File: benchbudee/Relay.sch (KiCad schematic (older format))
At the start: 0 parts

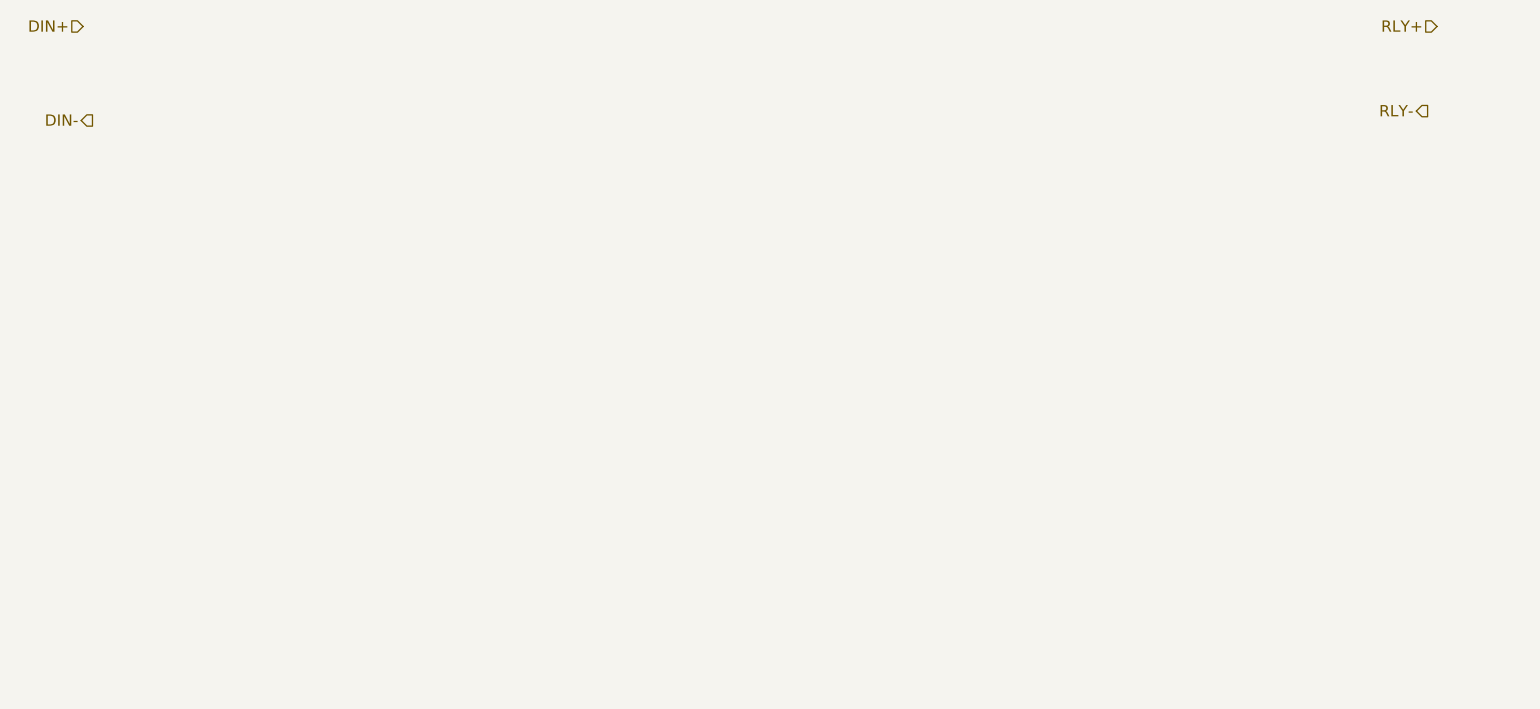
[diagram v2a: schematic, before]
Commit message: Added first pass at the relay module.
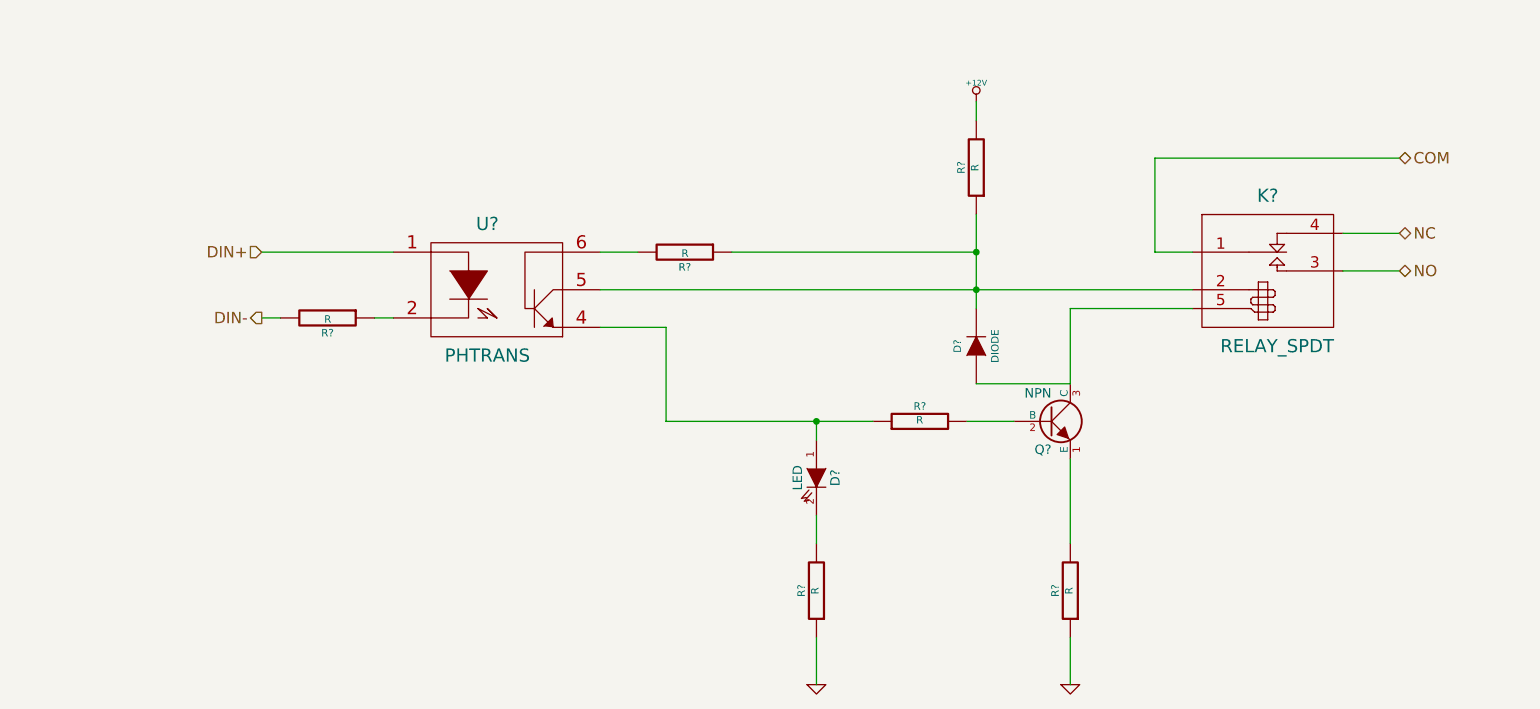
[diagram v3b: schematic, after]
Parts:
- added D?: LED, ~, symbol LED
- added D?: DIODE, ~, symbol DIODE
- added K?: RELAY_SPDT, ~, symbol RELAY_SPDT
- added Q?: NPN, ~, symbol NPN
- added R? (x6): R, ~, symbol R
- added U?: PHTRANS, ~, symbol PHTRANS
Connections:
- net DIN+: now also U?.1
- net DIN-: now also R?.2
- new net: R?.1, U?.2
- new net: D?.1 (A), R?.1, U?.4
- new net: D?.2 (K), K?.2 (COIL+), R?.1, R?.1, U?.5
- new net: R?.2, U?.6
- new net: Q?.2 (B), R?.2
- new net: Q?.1 (E), R?.2
- new net: D?.1 (A), K?.5 (COIL-), Q?.3 (C)
- new net: D?.2 (K), R?.2
- new net +12V: R?.2
- new net COM: K?.1 (COM)
- new net GND: R?.1, R?.1
- new net NC: K?.4 (NC)
- new net NO: K?.3 (NO)
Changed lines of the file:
@@
 LIBS:contrib
 LIBS:valves
+LIBS:benchbudee-custom
 LIBS:benchbudee-cache
 EELAYER 27 0
@@
 Comment4 ""
 $EndDescr
-Text HLabel 9050 1700 0    60   Input ~ 0
-RLY+
-Text HLabel 9000 2150 0    60   Output ~ 0
-RLY-
-Text HLabel 1850 1700 0    60   Input ~ 0
+Text HLabel 8850 2800 2    60   BiDi ~ 0
+NC
+Text HLabel 8850 3000 2    60   BiDi ~ 0
+NO
+Text HLabel 2800 2900 0    60   Input ~ 0
 DIN+
-Text HLabel 1900 2200 0    60   Output ~ 0
+Text HLabel 2800 3250 0    60   Output ~ 0
 DIN-
+$Comp
+L PHTRANS U?
+U 1 1 52FBF340
+P 4050 3100
+F 0 "U?" H 4000 3450 70  0000 C CNN
+F 1 "PHTRANS" H 4000 2750 70  0000 C CNN
+F 2 "~" H 4050 3100 60  0000 C CNN
+F 3 "~" H 4050 3100 60  0000 C CNN
+	1    4050 3100
+	1    0    0    -1
+$EndComp
+$Comp
+L R R?
+U 1 1 52FBF34F
+P 6300 3800
+F 0 "R?" V 6380 3800 40  0000 C CNN
+F 1 "R" V 6307 3801 40  0000 C CNN
+F 2 "~" V 6230 3800 30  0000 C CNN
+F 3 "~" H 6300 3800 30  0000 C CNN
+	1    6300 3800
+	0    -1   -1   0
+$EndComp
+$Comp
+L NPN Q?
+U 1 1 52FBF35E
+P 7000 3800
+F 0 "Q?" H 7000 3650 50  0000 R CNN
+F 1 "NPN" H 7000 3950 50  0000 R CNN
+F 2 "~" H 7000 3800 60  0000 C CNN
+F 3 "~" H 7000 3800 60  0000 C CNN
+	1    7000 3800
+	1    0    0    -1
+$EndComp
+$Comp
+L LED D?
+U 1 1 52FBF377
+P 5750 4100
+F 0 "D?" H 5750 4200 50  0000 C CNN
+F 1 "LED" H 5750 4000 50  0000 C CNN
+F 2 "~" H 5750 4100 60  0000 C CNN
+F 3 "~" H 5750 4100 60  0000 C CNN
+	1    5750 4100
+	0    1    1    0
+$EndComp
+Wire Wire Line
+	2800 2900 3500 2900
+$Comp
+L RELAY_SPDT K?
+U 1 1 52FBFAA6
+P 8150 3000
+F 0 "K?" H 8150 3400 70  0000 C CNN
+F 1 "RELAY_SPDT" H 8200 2600 70  0000 C CNN
+F 2 "~" H 8150 3150 60  0000 C CNN
+F 3 "~" H 8150 3150 60  0000 C CNN
+	1    8150 3000
+	1    0    0    -1
+$EndComp
+Text HLabel 8850 2400 2    60   BiDi ~ 0
+COM
+Wire Wire Line
+	7550 2900 7750 2900
+Wire Wire Line
+	8550 2800 8850 2800
+Wire Wire Line
+	8550 3000 8850 3000
+Wire Wire Line
+	7550 2900 7550 2400
+Wire Wire Line
+	7550 2400 8850 2400
+Wire Wire Line
+	4600 3300 4950 3300
+Wire Wire Line
+	4950 3300 4950 3800
+Wire Wire Line
+	4950 3800 5750 3800
+Wire Wire Line
+	5750 3800 6050 3800
+Wire Wire Line
+	6550 3800 6800 3800
+Wire Wire Line
+	7750 3200 7100 3200
+Wire Wire Line
+	7100 3200 7100 3600
+$Comp
+L R R?
+U 1 1 52FBFB64
+P 7100 4700
+F 0 "R?" V 7180 4700 40  0000 C CNN
+F 1 "R" V 7107 4701 40  0000 C CNN
+F 2 "~" V 7030 4700 30  0000 C CNN
+F 3 "~" H 7100 4700 30  0000 C CNN
+	1    7100 4700
+	-1   0    0    1
+$EndComp
+Wire Wire Line
+	7100 4000 7100 4450
+$Comp
+L GND #PWR?
+U 1 1 52FBFB7C
+P 7100 5200
+F 0 "#PWR?" H 7100 5200 30  0001 C CNN
+F 1 "GND" H 7100 5130 30  0001 C CNN
+F 2 "" H 7100 5200 60  0000 C CNN
+F 3 "" H 7100 5200 60  0000 C CNN
+	1    7100 5200
+	1    0    0    -1
+$EndComp
+Wire Wire Line
+	7100 4950 7100 5200
+$Comp
+L R R?
+U 1 1 52FBFBA4
+P 5750 4700
+F 0 "R?" V 5830 4700 40  0000 C CNN
+F 1 "R" V 5757 4701 40  0000 C CNN
+F 2 "~" V 5680 4700 30  0000 C CNN
+F 3 "~" H 5750 4700 30  0000 C CNN
+	1    5750 4700
+	-1   0    0    1
+$EndComp
+Wire Wire Line
+	5750 3900 5750 3800
+Connection ~ 5750 3800
+Wire Wire Line
+	5750 4450 5750 4300
+$Comp
+L GND #PWR?
+U 1 1 52FBFBD1
+P 5750 5200
+F 0 "#PWR?" H 5750 5200 30  0001 C CNN
+F 1 "GND" H 5750 5130 30  0001 C CNN
+F 2 "" H 5750 5200 60  0000 C CNN
+F 3 "" H 5750 5200 60  0000 C CNN
+	1    5750 5200
+	1    0    0    -1
+$EndComp
+Wire Wire Line
+	5750 4950 5750 5200
+$Comp
+L +12V #PWR?
+U 1 1 52FBFBEF
+P 6600 2100
+F 0 "#PWR?" H 6600 2050 20  0001 C CNN
+F 1 "+12V" H 6600 2200 30  0000 C CNN
+F 2 "" H 6600 2100 60  0000 C CNN
+F 3 "" H 6600 2100 60  0000 C CNN
+	1    6600 2100
+	1    0    0    -1
+$EndComp
+$Comp
+L R R?
+U 1 1 52FBFC4A
+P 6600 2450
+F 0 "R?" V 6680 2450 40  0000 C CNN
+F 1 "R" V 6607 2451 40  0000 C CNN
+F 2 "~" V 6530 2450 30  0000 C CNN
+F 3 "~" H 6600 2450 30  0000 C CNN
+	1    6600 2450
+	-1   0    0    1
+$EndComp
+Wire Wire Line
+	6600 2100 6600 2200
+Wire Wire Line
+	6600 2700 6600 2900
+Wire Wire Line
+	6600 2900 6600 3100
+Wire Wire Line
+	6600 3100 6600 3200
+Wire Wire Line
+	4600 3100 6600 3100
+Wire Wire Line
+	6600 3100 7750 3100
+Connection ~ 6600 3100
+$Comp
+L R R?
+U 1 1 52FBFCA0
+P 5050 2900
+F 0 "R?" V 5130 2900 40  0000 C CNN
+F 1 "R" V 5057 2901 40  0000 C CNN
+F 2 "~" V 4980 2900 30  0000 C CNN
+F 3 "~" H 5050 2900 30  0000 C CNN
+	1    5050 2900
+	0    1    1    0
+$EndComp
+Wire Wire Line
+	4600 2900 4800 2900
+$Comp
+L R R?
+U 1 1 52FBFCE0
+P 3150 3250
+F 0 "R?" V 3230 3250 40  0000 C CNN
+F 1 "R" V 3157 3251 40  0000 C CNN
+F 2 "~" V 3080 3250 30  0000 C CNN
+F 3 "~" H 3150 3250 30  0000 C CNN
+	1    3150 3250
+	0    1    1    0
+$EndComp
+Wire Wire Line
+	2800 3250 2900 3250
+Wire Wire Line
+	3400 3250 3500 3250
+$Comp
+L DIODE D?
+U 1 1 52FBFD41
+P 6600 3400
+F 0 "D?" H 6600 3500 40  0000 C CNN
+F 1 "DIODE" H 6600 3300 40  0000 C CNN
+F 2 "~" H 6600 3400 60  0000 C CNN
+F 3 "~" H 6600 3400 60  0000 C CNN
+	1    6600 3400
+	0    -1   -1   0
+$EndComp
+Wire Wire Line
+	7100 3600 6600 3600
+Wire Wire Line
+	5300 2900 6600 2900
+Connection ~ 6600 2900
 $EndSCHEMATC

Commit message: Added Power Adjustment sheet.  Populated power sheet.
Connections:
- net +12V renamed +12P
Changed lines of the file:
@@
 $Descr A4 11693 8268
 encoding utf-8
-Sheet 4 8
+Sheet 4 9
 Title ""
-Date "12 feb 2014"
+Date "13 feb 2014"
 Rev ""
 Comp ""
@@
 	5750 4950 5750 5200
 $Comp
-L +12V #PWR?
-U 1 1 52FBFBEF
-P 6600 2100
-F 0 "#PWR?" H 6600 2050 20  0001 C CNN
-F 1 "+12V" H 6600 2200 30  0000 C CNN
-F 2 "" H 6600 2100 60  0000 C CNN
-F 3 "" H 6600 2100 60  0000 C CNN
-	1    6600 2100
-	1    0    0    -1
-$EndComp
-$Comp
 L R R?
 U 1 1 52FBFC4A
@@
 	5300 2900 6600 2900
 Connection ~ 6600 2900
+$Comp
+L +12P #PWR?
+U 1 1 52FC18D7
+P 6600 2100
+F 0 "#PWR?" H 6600 2070 30  0001 C CNN
+F 1 "+12P" H 6600 2200 30  0000 C CNN
+F 2 "" H 6600 2100 60  0000 C CNN
+F 3 "" H 6600 2100 60  0000 C CNN
+	1    6600 2100
+	1    0    0    -1
+$EndComp
 $EndSCHEMATC

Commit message: Setting up for layout
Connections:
- net COM renamed RELAY_COM
- net DIN+ renamed RELAY+
- net DIN- renamed RELAY-
- net NC renamed RELAY_NC
- net NO renamed RELAY_NO
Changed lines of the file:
@@
 LIBS:benchbudee-custom
 LIBS:benchbudee-cache
-EELAYER 27 0
+EELAYER 24 0
 EELAYER END
 $Descr A4 11693 8268
 encoding utf-8
-Sheet 4 9
+Sheet 3 9
 Title ""
 Date "14 feb 2014"
@@
 $EndDescr
 Text HLabel 8850 2800 2    60   BiDi ~ 0
-NC
+RELAY_NC
 Text HLabel 8850 3000 2    60   BiDi ~ 0
-NO
+RELAY_NO
 Text HLabel 2800 2900 0    60   Input ~ 0
-DIN+
+RELAY+
 Text HLabel 2800 3250 0    60   Output ~ 0
-DIN-
+RELAY-
 $Comp
 L PHTRANS U?
@@
 $EndComp
 Text HLabel 8850 2400 2    60   BiDi ~ 0
-COM
+RELAY_COM
 Wire Wire Line
 	7550 2900 7750 2900

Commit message: Relay module footprints done
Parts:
- removed R?: R, ~, symbol R
- removed U?: PHTRANS, ~, symbol PHTRANS
- added R5: 0, ~, symbol R
- added U1: LTV-816S, symbol OPTO-TRANSISTOR4
- D1: renamed from D?; value LED -> LG 0971-KN-1; MFG Part Number (none) -> LG 0971-KN-1
- D2: renamed from D?; value DIODE -> B130-13-F
- K1: renamed from K?; value RELAY_SPDT -> 1461069-5; MFG Part Number (none) -> 1461069-5
- Q1: renamed from Q?; value NPN -> 2N3904; MFG Part Number (none) -> MM8T3904-7-F
- R1: renamed from R?; value R -> 500
- R2: renamed from R?; value R -> 200
- R3, R6: renamed from R?; value R -> 0
- R4: renamed from R?; value R -> 100
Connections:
- net +12P: now also R5.2
- net RELAY+: now also U1.1 (A)
- net at R1.1: now also U1.2 (K)
- net at D1.1 (A), R4.1: now also U1.3 (E)
- net at D2.2 (K), K1.2 (COIL+): now also R5.1; no longer R3.1
- new net: R3.1, U1.4 (C)
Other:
- moved on the sheet: D1, D2, Q1, R1, R2, R3, R4, R6
